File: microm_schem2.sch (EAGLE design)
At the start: 44 parts, among them IC1 DSPIC33FJ64MC804-PT, IC2 LD117AV33, IC3 7805T, IC4 RN4871-I_RM140, IC5 TB6612FNG,C,8,EL, IC6 LK112SM50TR, IC7 LK112SM33TR, Q1 16 MHz

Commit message: Update schematics and library.
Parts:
- removed C15, C16: C0805C104K4JACAUTO, SamacSys_Parts:C0805C104K4JACAUTO
- removed C21: C0805C225K4RAC3123, SamacSys_Parts:C0805C225K4RAC3123
- removed G1: AB9V, battery:AB9V
- removed IC3: 7805T, linear:7805T
- removed IC4: RN4871-I_RM140, SamacSys_Parts:RN4871-I_RM140
- removed IC6: LK112SM50TR, SamacSys_Parts:LK112SM50TR
- removed IC7: LK112SM33TR, SamacSys_Parts:LK112SM33TR
- added C1, C2: TL8W9226M010C, SamacSys_Parts:TL8W9226M010C
- added C4, C5: TAJP106K010RNJ, SamacSys_Parts:TAJP106K010RNJ
- added C6: C0805C104K4JACAUTO, SamacSys_Parts:C0805C104K4JACAUTO
- added C7: GCM21BR71A106KE22L, SamacSys_Parts:GCM21BR71A106KE22L
- added C9: 1uF, rcl:C-EUC0805
- added CON1: XT60PW-M, amass:XT60PW-M
- added IC8: LM1117DTX-5.0_NOPB, SamacSys_Parts:LM1117DTX-5.0_NOPB
- added IC9: LM1117DTX-3.3_NOPB, SamacSys_Parts:LM1117DTX-3.3_NOPB
- added LED1: APT2012MGC, SamacSys_Parts:APT2012MGC
- added LED6: APT2012VBC_D, SamacSys_Parts:APT2012VBC_D
- added R1: ERJ-PB6B2700V, rcl:R-EU_R0805
- added R2: ERJ-PB6B1001V, SamacSys_Parts:ERJ-PB6B1001V
- added R3, R4: ERJ-PB6B1002V, SamacSys_Parts:ERJ-PB6B1002V
- added S1: TS04-66-95-BK-160-SMT-TR, SamacSys_Parts:TS04-66-95-BK-160-SMT-TR
- added S2: 1101M2S3CQE2, SamacSys_Parts:1101M2S3CQE2
- C8: value 10 uF -> (none)
- IC2: value LD117AV33 -> RN4871-I_RM140; device v-reg:LD117AV33 -> SamacSys_Parts:RN4871-I_RM140
- S3, S4: value SKHMPSE010 -> TS04-66-95-BK-160-SMT-TR; device switch:SKHMPSE010 -> SamacSys_Parts:TS04-66-95-BK-160-SMT-TR
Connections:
- net AO1 renamed MA_OUT1
- net AO2 renamed MA_OUT2
- net BO1 renamed MB_OUT1
- net BO2 renamed MB_OUT2
- net BUTTON renamed BUTTON1
- net DIR_A1 renamed MA_DIR2
- net DIR_A2 renamed MA_DIR1
- net DIR_B1 renamed MB_DIR1
- net DIR_B2 renamed MB_DIR2
- net ENCA_A renamed MA_ENC_A
- net ENCA_B renamed MA_ENC_B
- net ENCB_A renamed MB_ENC_A
- net ENCB_B renamed MB_ENC_B
- net N$20 renamed SENS_DIST_3
- net N$21 renamed SENS_DIST_2
- net N$22 renamed SENS_DIST_1
- net N$5 renamed PGED1
- net N$6 renamed PGEC1
- net STDBY renamed M_STDBY
- removed net 26: IC1.AN7/RP17/CN9/RC1
- removed net 27: IC1.AN8/CVREF/RP18/PMA2/CN10/RC2
- removed net VDD3: IC5.VCC
- removed net VM: IC5.VM1
- new net BT_RESET: C9.1, IC2.RST_N, R4.1
- new net BT_STATUS: IC2.P0_2, LED6.K
- new net BUTTON2: R2.2
- new net MAB_V: C6.1, C7.1, IC5.VM1
- new net N$13: C4.+, IC8.ADJ/GND
- new net N$5: C8.1, R2.1, R3.1, S4.COM_1, S4.COM_2
- new net UART_CTS: IC2.P0_0, UART.6
- new net UART_RTS: IC2.P3_6, UART.3
- new net UART_RX: IC1.AN7/RP17/CN9/RC1, IC2.UART_RX, UART.4
- new net UART_TX: IC1.AN8/CVREF/RP18/PMA2/CN10/RC2, IC2.UART_TX, UART.5
- net +3V3: now also C2.+, IC2.VBAT, IC5.VCC, IC9.OUTPUT/VOUT, LED6.A, R3.2, R4.2, UART.1; no longer C8.1, IC2.OUT, UART.4, UART.5
- net +5V: now also C1.+, IC8.TAB_(VOUT), IC9.INPUT; no longer C15.2, C16.2, IC2.IN, IC3.VO
- net GND: now also C1.-, C17.1, C18.1, C19.1, C2.-, C20.1, C4.-, C5.-, C6.2, C7.2, C8.2, C9.2, CON1.-, IC2.GND_1, IC2.GND_2, LED1.K, S1.NO_1, S1.NO_2, S3.NO_1, S3.NO_2, S4.NO_1, S4.NO_2, UART.2; no longer S3.1.1, S3.1.2, S3.SH, S4.1.1, S4.1.2, S4.SH
- net MCLR: now also S1.COM_1, S1.COM_2; no longer S3.2.1, S3.2.2
- net N$1: now also S3.COM_1, S3.COM_2; no longer S4.2.1, S4.2.2
- net N$11: now also C5.+, IC9.ADJ/GND; no longer C15.1, C16.1, C17.1, C18.1, C19.1, C20.1, C21.1, C8.2, G1.-, IC2.ADJ, IC3.GND
- net N$2: now also CON1.+, S2.3; no longer IC1.SCL1/RP8/CN22/PMD4/RB8, UART.2
- net N$4: now also LED1.A, R1.2; no longer IC1.INT0/RP7/CN23/PMD5/RB7, UART.3
- net V+: now also IC8.INPUT, R1.1, S2.2; no longer C21.2, G1.+, IC3.VI
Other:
- note added: "Buttons"
- note added: "Distance Sensors"
- note added: "LEDs"
- note added: "Linear Voltage Regulator"
- note added: "Motor Control"
- note added: "Oscillator"
- note added: "Program Header"
- note added: "Reset Switch"
- note added: "TODO:"
- note added: "TODO: Capacitors - which ones?"
- note added: "TODO: Dummy capacitor, but need 1uF ceramic"
- note added: "TODO: Why do we need this circuit?"
- note added: "uC"
- moved on the sheet: C12, C13, C14, C17, C18, C19, C20, C22, C23, C3, C8, D2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

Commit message: Add IMU and LCD, complete wiring and clean up.
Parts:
- removed C23: C0805C200J5GACAUTO, SamacSys_Parts:C0805C200J5GACAUTO
- removed IC1: DSPIC33FJ64MC804-PT, microchip-dspic33fjxxmc:DSPIC33FJ64MC804-PT
- removed IC2: RN4871-I_RM140, SamacSys_Parts:RN4871-I_RM140
- removed IC5: TB6612FNG,C,8,EL, SamacSys_Parts:TB6612FNG,C,8,EL
- removed IC8: LM1117DTX-5.0_NOPB, SamacSys_Parts:LM1117DTX-5.0_NOPB
- removed IC9: LM1117DTX-3.3_NOPB, SamacSys_Parts:LM1117DTX-3.3_NOPB
- removed JP1, JP2, JP3: (no value), pinhead:PINHD-1X3
- removed LED1: APT2012MGC, SamacSys_Parts:APT2012MGC
- removed LED6: APT2012VBC_D, SamacSys_Parts:APT2012VBC_D
- removed R14: ERJ-PB6B1002V, SamacSys_Parts:ERJ-PB6B1002V
- removed S3, S4: TS04-66-95-BK-160-SMT-TR, SamacSys_Parts:TS04-66-95-BK-160-SMT-TR
- added 3.3V, 5V, 7.4V: green, 20mA, 2.5V, led:LEDCHIP-LED0805
- added BT_STATUS: blue, 20mA, 3.3V, led:LEDCHIP-LED0805
- added C10, C11, C15, C16, C21: 100nF, 10-20V, low-esr, rcl:C-EUC0805
- added I2C: (no value), pinhead:PINHD-1X4
- added IC3: SIP32432DR3-T1GE3, SamacSys_Parts:SIP32432DR3-T1GE3
- added IMU_1, IMU_2: (no value), pinhead:PINHD-1X6
- added LCD: (no value), pinhead:PINHD-1X11
- added LS1: CPT-9019A-SMT-TR, SamacSys_Parts:CPT-9019A-SMT-TR
- added MOTOR_CTL: TB6612FNG,C,8,EL, SamacSys_Parts:TB6612FNG,C,8,EL
- added POWER_SW: 1101M2S3CQE2, SamacSys_Parts:1101M2S3CQE2
- added R5, R6, R7: 47Ω, rcl:R-EU_R0805
- added RESET: TS04-66-95-BK-160-SMT-TR, SamacSys_Parts:TS04-66-95-BK-160-SMT-TR
- added SENS_DIST_1, SENS_DIST_2, SENS_DIST_3: (no value), pinhead:PINHD-1X3
- added SPI: (no value), pinhead:PINHD-2X4
- added TP_3.3V, TP_5V, TP_7.4V, TP_GND, TP_OSC: (no value), pinhead:PINHD-1X1
- added UART_BT: RN4871-I_RM140, SamacSys_Parts:RN4871-I_RM140
- added UC: DSPIC33FJ64MC804-PT, microchip-dspic33fjxxmc:DSPIC33FJ64MC804-PT
- added VR_3.3V: LM1117DTX-3.3_NOPB, SamacSys_Parts:LM1117DTX-3.3_NOPB
- added VR_5V: LM1117DTX-5.0_NOPB, SamacSys_Parts:LM1117DTX-5.0_NOPB
- C1: value TL8W9226M010C -> 10uF, tantalum; device SamacSys_Parts:TL8W9226M010C -> rcl:C-EUC0805
- C12, C13, C14: value (none) -> 10 uF
- C17, C18: value C0805C104K4JACAUTO -> 20pF, low-esr, ceramic; device SamacSys_Parts:C0805C104K4JACAUTO -> rcl:C-EUC0805
- C19, C6: value C0805C104K4JACAUTO -> 100nF; device SamacSys_Parts:C0805C104K4JACAUTO -> rcl:C-EUC0805
- C2: value TL8W9226M010C -> 22uF, tantalum, esr 0.3-22Ω; device SamacSys_Parts:TL8W9226M010C -> rcl:C-EUC0805
- C20: value C0805C104K4JACAUTO -> 10uF; device SamacSys_Parts:C0805C104K4JACAUTO -> rcl:C-EUC0805
- C22: value C0805C200J5GACAUTO -> 100nF, 10-20V, low-esr; device SamacSys_Parts:C0805C200J5GACAUTO -> rcl:C-EUC0805
- C3, C8: value (none) -> 100nF
- C4: value TAJP106K010RNJ -> 10uF, tantalum; device SamacSys_Parts:TAJP106K010RNJ -> rcl:C-EUC0805
- C5: value TAJP106K010RNJ -> 22uF, tantalum, esr 0.3-22Ω; device SamacSys_Parts:TAJP106K010RNJ -> rcl:C-EUC0805
- C7: value GCM21BR71A106KE22L -> 10uF; device SamacSys_Parts:GCM21BR71A106KE22L -> rcl:C-EUC0805
- LED2, LED3, LED4, LED5: value (none) -> red, 20mA, 2.5V
- R1: value ERJ-PB6B2700V -> 270Ω
- R10, R3, R4, R9: value ERJ-PB6B1002V -> 10kΩ; device SamacSys_Parts:ERJ-PB6B1002V -> rcl:R-EU_R0805
- R11: value ERJ-PB6B1002V -> 47Ω; device SamacSys_Parts:ERJ-PB6B1002V -> rcl:R-EU_R0805
- R12, R13: value ERJ-PB6B1002V -> 270Ω; device SamacSys_Parts:ERJ-PB6B1002V -> rcl:R-EU_R0805
- R2, R8: value ERJ-PB6B1001V -> 1kΩ; device SamacSys_Parts:ERJ-PB6B1001V -> rcl:R-EU_R0805
- S2: value 1101M2S3CQE2 -> TS04-66-95-BK-160-SMT-TR; device SamacSys_Parts:1101M2S3CQE2 -> SamacSys_Parts:TS04-66-95-BK-160-SMT-TR
- UART: value MICS-SMD06 -> (none); device con-lumberg:MICS-SMD06 -> pinhead:PINHD-1X4
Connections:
- removed net 1: IC1.SDA1/RP9/CN21/PMD3/RB9
- removed net 11: IC1.PWM1L2/DAC1RN/RP13/CN13/PMRD/RB13
- removed net 12: IC1.TMS/PMA10/RA10
- removed net 15: IC1.PWM1L1/RP15/CN11/PMCS1/RB15
- removed net 2: IC1.PWM2H1/RP22/CN18/PMA1/RC6
- removed net 23: IC1.AN4/C1IN-/RP2/CN6/RB2
- removed net 24: IC1.AN5/C1IN+/RP3/CN7/RB3
- removed net 25: IC1.AN6/RP16/CN8/RC0
- removed net 3: IC1.PWM2L1/RP23/CN17/PMA0/RC7
- removed net 34: IC1.SOSCO/T1CK/CN0/RA4
- removed net 35: IC1.TDI/PMA9/RA9
- removed net MAB_V: C6.1, C7.1, IC5.VM1
- removed net N$12: IC1.AN0/VREF+/CN2/RA0
- removed net N$14: IC5.VM2
- removed net N$15: IC5.VM3
- removed net N$29: MOTOR_B.4
- removed net N$5: C8.1, R2.1, R3.1, S4.COM_1, S4.COM_2
- removed net PGEC1: IC1.PGEC1/AN3/C2IN+/RP1/CN5/RB1, PROGRAM.5
- removed net PGED1: IC1.PGED1/AN2/C2IN-/RP0/CN4/RB0, PROGRAM.4
- removed net UART_CTS: IC2.P0_0, UART.6
- removed net UART_RTS: IC2.P3_6, UART.3
- removed net V+: IC8.INPUT, R1.1, S2.2
- removed net VDD33: MOTOR_A.4
- new net +7V4: POWER_SW.2, R1.1, TP_7.4V.1, VR_5V.INPUT
- new net AGND: UC.AVSS
- new net BUZZ_PWM: LS1.+, UC.PWM2H1/RP22/CN18/PMA1/RC6
- new net GND1: 5V.C
- new net GND2: 3.3V.C
- new net I2C_SCL: I2C.1, IMU_2.4, UC.SCL1/RP8/CN22/PMD4/RB8
- new net I2C_SDA: I2C.2, IMU_2.5, UC.SDA1/RP9/CN21/PMD3/RB9
- new net IMU_INT: IMU_2.6, UC.INT0/RP7/CN23/PMD5/RB7
- new net LCD_BL_PWM: LCD.11, UC.PGED2/PWM1H3/RP10/CN16/PMD2/RB10
- new net LCD_RESET: LCD.8, UC.SOSCI/RP4/CN1/RB4
- new net M_3V3: MOTOR_CTL.VCC
- new net M_7V4: C6.1, C7.1, MOTOR_CTL.VM1, MOTOR_CTL.VM2, MOTOR_CTL.VM3
- new net N$16: 5V.A, R12.2
- new net N$17: 3.3V.A, R13.2
- new net N$6: C3.1, R8.1, R9.1, S1.COM_1, S1.COM_2
- new net PG_EC1: PROGRAM.5, UC.PGEC1/AN3/C2IN+/RP1/CN5/RB1
- new net PG_ED1: PROGRAM.4, UC.PGED1/AN2/C2IN-/RP0/CN4/RB0
- new net SENS_DIST_ON: IC3.ON/OFF, UC.TDO/PMA8/RA8
- new net SENS_DIST_V: C12.1, C13.1, C14.1, IC3.OUT, SENS_DIST_1.1, SENS_DIST_2.1, SENS_DIST_3.1
- new net SPI_DBG_CS: SPI.6
- new net SPI_LCD_CS: LCD.7, SPI.2, UC.AN6/RP16/CN8/RC0
- new net SPI_LCD_DC: LCD.9, UC.AN8/CVREF/RP18/PMA2/CN10/RC2
- new net SPI_SCK: LCD.4, SPI.1, UC.PGEC2/PWM1L3/RP11/CN15/PMD1/RB11
- new net SPI_SDI: LCD.6, SPI.5, UC.PWM1L2/DAC1RN/RP13/CN13/PMRD/RB13
- new net SPI_SDO: LCD.5, SPI.3, UC.PWM1L1/RP15/CN11/PMCS1/RB15
- new net SPI_SD_CS: LCD.10, SPI.4
- net +3V3: now also BT_STATUS.C, C10.1, C11.1, C15.1, C16.1, C19.1, C20.1, C21.1, C22.1, C5.1, I2C.4, IMU_2.1, LCD.1, MOTOR_A.4, MOTOR_B.4, R11.1, R13.1, R5.1, R6.1, R7.1, SPI.7, TP_3.3V.1, UART.4, UART_BT.VBAT, UC.AVDD, UC.VCAP/VDDCORE, UC.VDD, UC.VDD1, VR_3.3V.OUTPUT/VOUT; no longer C17.2, C18.2, C19.2, C2.+, C20.2, IC1.AVDD, IC1.VCAP/VDDCORE, IC1.VDD, IC1.VDD1, IC2.VBAT, IC5.VCC, IC9.OUTPUT/VOUT, LED6.A, R11.2, R12.2, R13.2, R14.2, UART.1
- net +5V: now also C2.1, IC3.IN, R12.1, TP_5V.1, VR_3.3V.INPUT, VR_5V.TAB_(VOUT); no longer C1.+, C12.1, C13.1, C14.1, IC8.TAB_(VOUT), IC9.INPUT, JP1.1, JP2.1, JP3.1
- net 0SC2: now also C18.1, TP_OSC.1; no longer C22.2
- net BT_RESET: now also UART_BT.RST_N; no longer IC2.RST_N
- net BT_STATUS: now also BT_STATUS.A, UART_BT.P0_2; no longer IC2.P0_2, LED6.K
- net BUTTON1: now also UC.PWM2L1/RP23/CN17/PMA0/RC7
- net GND: now also 7.4V.C, C1.2, C10.2, C11.2, C15.2, C16.2, C17.2, C18.2, C19.2, C2.2, C20.2, C21.2, C22.2, C4.2, C5.2, I2C.3, IC3.GND_1, IC3.GND_2, IMU_1.4, IMU_2.3, LCD.3, LS1.-, MOTOR_CTL.GND, MOTOR_CTL.PGND1_1, MOTOR_CTL.PGND1_2, MOTOR_CTL.PGND2_1, MOTOR_CTL.PGND2_2, RESET.NO_1, RESET.NO_2, S2.NO_1, S2.NO_2, SENS_DIST_1.2, SENS_DIST_2.2, SENS_DIST_3.2, SPI.8, TP_GND.1, UART.3, UART_BT.GND_1, UART_BT.GND_2, UC.VSS, UC.VSS1, UC.VSS2; no longer C1.-, C17.1, C18.1, C19.1, C2.-, C20.1, C22.1, C23.1, C4.-, C5.-, IC1.AVSS, IC1.VSS, IC1.VSS1, IC1.VSS2, IC2.GND_1, IC2.GND_2, IC5.GND, IC5.PGND1_1, IC5.PGND1_2, IC5.PGND2_1, IC5.PGND2_2, JP1.2, JP2.2, JP3.2, LED1.K, S3.NO_1, S3.NO_2, S4.NO_1, S4.NO_2, UART.2
- net LED1: now also UC.AN0/VREF+/CN2/RA0
- net LED2: now also UC.AN1/VREF-/CN3/RA1
- net MA_DIR1: now also MOTOR_CTL.AIN1, UC.TMS/PMA10/RA10; no longer IC5.AIN1
- net MA_DIR2: now also MOTOR_CTL.AIN2, UC.TCK/PMA7/RA7; no longer IC5.AIN2
- net MA_ENC_A: now also UC.RP19/CN28/PMBE/RC3; no longer IC1.RP19/CN28/PMBE/RC3
- net MA_ENC_B: now also UC.RP20/CN25/PMA4/RC4; no longer IC1.RP20/CN25/PMA4/RC4
- net MA_OUT1: now also MOTOR_CTL.AO1_1, MOTOR_CTL.AO1_2; no longer IC5.AO1_1, IC5.AO1_2
- net MA_OUT2: now also MOTOR_CTL.AO2_1, MOTOR_CTL.AO2_2; no longer IC5.AO2_1, IC5.AO2_2
- net MA_PWM: now also MOTOR_CTL.PWMA, UC.PWM1H1/RTCC/RP14/CN12/PMWR/RB14; no longer IC1.PWM1H1/RTCC/RP14/CN12/PMWR/RB14, IC5.PWMA
- net MB_DIR1: now also MOTOR_CTL.BIN1, UC.SOSCO/T1CK/CN0/RA4; no longer IC5.BIN1
- net MB_DIR2: now also MOTOR_CTL.BIN2, UC.TDI/PMA9/RA9; no longer IC5.BIN2
- net MB_ENC_A: now also UC.RP24/CN20/PMA5/RC8; no longer IC1.RP24/CN20/PMA5/RC8
- net MB_ENC_B: now also UC.RP25/CN19/PMA6/RC9; no longer IC1.RP25/CN19/PMA6/RC9
- net MB_OUT1: now also MOTOR_CTL.BO1_1, MOTOR_CTL.BO1_2; no longer IC5.BO1_1, IC5.BO1_2
- net MB_OUT2: now also MOTOR_CTL.BO2_1, MOTOR_CTL.BO2_2; no longer IC5.BO2_1, IC5.BO2_2
- net MB_PWM: now also MOTOR_CTL.PWMB, UC.PWM1H2/DAC1RP/RP12/CN14/PMD0/RB12; no longer IC1.PWM1H2/DAC1RP/RP12/CN14/PMD0/RB12, IC5.PWMB
- net MCLR: now also RESET.COM_1, RESET.COM_2, UC.MCLR; no longer IC1.MCLR, S1.COM_1, S1.COM_2
- net M_STDBY: now also MOTOR_CTL.STBY, UC.RP21/CN26/PMA3/RC5; no longer IC1.RP21/CN26/PMA3/RC5, IC5.STBY
- net N$1: now also C8.1, R2.1, R3.1, S2.COM_1, S2.COM_2; no longer C3.1, R8.1, R9.1, S3.COM_1, S3.COM_2
- net N$10: now also R11.2; no longer R14.1
- net N$11: now also C4.1, VR_3.3V.ADJ/GND; no longer C5.+, IC9.ADJ/GND
- net N$13: now also C1.1, VR_5V.ADJ/GND; no longer C4.+, IC8.ADJ/GND
- net N$2: now also POWER_SW.3; no longer S2.3
- net N$3: now also R5.2; no longer R11.1
- net N$4: now also 7.4V.A; no longer LED1.A
- net N$8: now also R6.2; no longer R12.1
- net N$9: now also R7.2; no longer R13.1
- net OSC1: now also C17.1, UC.OSC1/CLKI/CN30/RA2; no longer C23.2, IC1.OSC1/CLKI/CN30/RA2
- net OSC2: now also UC.OSC2/CLKO/CN29/RA3; no longer IC1.OSC2/CLKO/CN29/RA3
- net SENS_DIST_1: now also SENS_DIST_1.3, UC.AN4/C1IN-/RP2/CN6/RB2; no longer JP1.3
- net SENS_DIST_2: now also SENS_DIST_2.3, UC.AN5/C1IN+/RP3/CN7/RB3; no longer JP2.3
- net SENS_DIST_3: now also SENS_DIST_3.3, UC.AN7/RP17/CN9/RC1; no longer JP3.3
- net UART_RX: now also UART.1, UART_BT.UART_RX, UC.PGED3/ASDA1/RP5/CN27/PMD7/RB5; no longer IC1.AN7/RP17/CN9/RC1, IC2.UART_RX, UART.4
- net UART_TX: now also UART.2, UART_BT.UART_TX, UC.PGEC3/ASCL1/RP6/CN24/PMD6/RB6; no longer IC1.AN8/CVREF/RP18/PMA2/CN10/RC2, IC2.UART_TX, UART.5
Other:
- note added: "4x uC, 2x QEA"
- note added: "Debug Interfaces"
- note added: "IMU Header"
- note added: "LCD Header"
- note added: "Piezo Buzzer"
- note added: "TODO: Transistor/Load Switch correct?"
- note added: "UART"
- note removed: "TODO: Dummy capacitor, but need 1uF ceramic"
- moved on the sheet: C12, C13, C14, C3, C8, C9, CON1, D2, LED2, LED3, LED4, LED5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

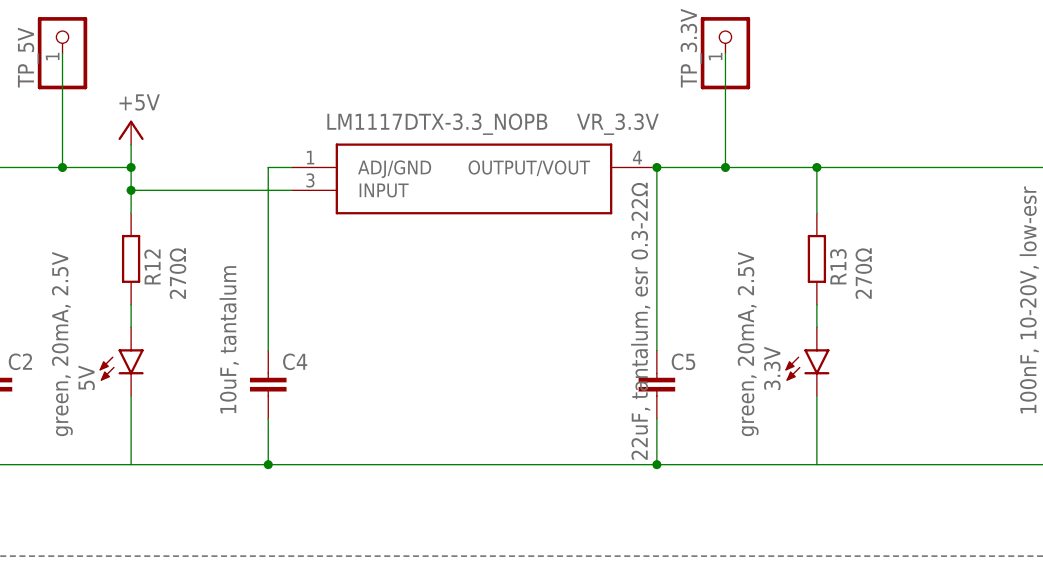
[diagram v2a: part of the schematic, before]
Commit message: Fix led resitors.
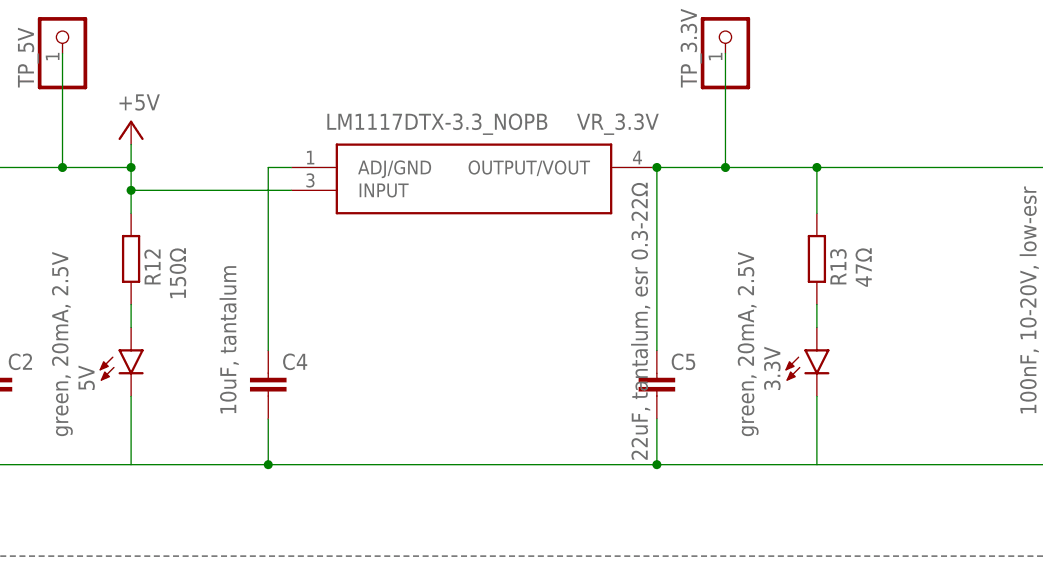
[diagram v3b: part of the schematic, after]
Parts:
- R12: value 270Ω -> 150Ω
- R13: value 270Ω -> 47Ω
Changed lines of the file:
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@@
 <part name="GND32" library="supply1" library_urn="urn:adsk.eagle:library:371" deviceset="GND" device=""/>
 <part name="UART" library="pinhead" library_urn="urn:adsk.eagle:library:325" deviceset="PINHD-1X4" device="" package3d_urn="urn:adsk.eagle:package:22407/2"/>
-<part name="R12" library="rcl" library_urn="urn:adsk.eagle:library:334" deviceset="R-EU_" device="R0805" package3d_urn="urn:adsk.eagle:package:23553/2" value="270Ω"/>
+<part name="R12" library="rcl" library_urn="urn:adsk.eagle:library:334" deviceset="R-EU_" device="R0805" package3d_urn="urn:adsk.eagle:package:23553/2" value="150Ω"/>
 <part name="5V" library="led" library_urn="urn:adsk.eagle:library:259" deviceset="LED" device="CHIP-LED0805" package3d_urn="urn:adsk.eagle:package:15818/2" value="green, 20mA, 2.5V"/>
-<part name="R13" library="rcl" library_urn="urn:adsk.eagle:library:334" deviceset="R-EU_" device="R0805" package3d_urn="urn:adsk.eagle:package:23553/2" value="270Ω"/>
+<part name="R13" library="rcl" library_urn="urn:adsk.eagle:library:334" deviceset="R-EU_" device="R0805" package3d_urn="urn:adsk.eagle:package:23553/2" value="47Ω"/>
 <part name="3.3V" library="led" library_urn="urn:adsk.eagle:library:259" deviceset="LED" device="CHIP-LED0805" package3d_urn="urn:adsk.eagle:package:15818/2" value="green, 20mA, 2.5V"/>
 <part name="BT_STATUS" library="led" library_urn="urn:adsk.eagle:library:259" deviceset="LED" device="CHIP-LED0805" package3d_urn="urn:adsk.eagle:package:15818/2" value="blue, 20mA, 3.3V"/>

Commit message: Fix ERC issues and add mounting pads.
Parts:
- added H1, H2, H3, H4, H5, H6, H7, H8: 2.8, holes:MOUNT-PAD-SQUARE2.8
- added R14: 0Ω, rcl:R-EU_R0805
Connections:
- removed net 0SC2: C18.1, Q1.2, TP_OSC.1
- removed net GND1: 5V.C
- removed net GND2: 3.3V.C
- removed net M_3V3: MOTOR_CTL.VCC
- removed net M_7V4: C6.1, C7.1, MOTOR_CTL.VM1, MOTOR_CTL.VM2, MOTOR_CTL.VM3
- removed net SPI_DBG_CS: SPI.6
- net +3V3: now also MOTOR_CTL.VCC
- net +7V4: now also C6.1, C7.1, MOTOR_CTL.VM1, MOTOR_CTL.VM2, MOTOR_CTL.VM3
- net AGND: now also R14.2
- net GND: now also 3.3V.C, 5V.C, H1.MOUNT, H2.MOUNT, H3.MOUNT, H4.MOUNT, H5.MOUNT, H6.MOUNT, H7.MOUNT, H8.MOUNT, R14.1
- net MA_ENC_A: now also MOTOR_A.6; no longer MOTOR_A.5
- net MA_ENC_B: now also MOTOR_A.5; no longer MOTOR_A.6
- net MA_OUT1: now also MOTOR_A.2; no longer MOTOR_A.1
- net MA_OUT2: now also MOTOR_A.1; no longer MOTOR_A.2
- net OSC2: now also C18.1, Q1.2, TP_OSC.1
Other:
- note added: "Hack: Fix ERC"
- note added: "Note: Reversed Voltage and QEI PINs as wheel is mounted in reverse position."
- moved on the sheet: IMU_1, IMU_2

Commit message: Add first version of the PCB.
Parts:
- removed H3, H4, H5, H6, H7, H8: 2.8, holes:MOUNT-PAD-SQUARE2.8
- removed LED5: red, 20mA, 2.5V, led:LEDCHIPLED_0805
- added LED1: red, 20mA, 2.5V, led:LEDCHIPLED_0805
- H1, H2: value 2.8 -> MOUNT-PAD-ROUND2.8; device holes:MOUNT-PAD-SQUARE2.8 -> holes:MOUNT-PAD-ROUND2.8
- PROGRAM: value MICS-SMD06 -> (none); device con-lumberg:MICS-SMD06 -> pinhead:PINHD-1X6/90
- renumbered CON1 to BAT, IC3 to T1, TP_3.3V to TP3V3, TP_5V to TP5V, TP_7.4V to TP7V4, TP_GND to TPGND
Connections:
- net GND: no longer H3.MOUNT, H4.MOUNT, H5.MOUNT, H6.MOUNT, H7.MOUNT, H8.MOUNT
- net LED1: now also LED1.C; no longer LED2.C
- net LED2: now also LED2.C; no longer LED5.C
- net N$3: now also LED1.A; no longer LED2.A
- net N$8: now also LED2.A; no longer LED5.A
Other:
- moved on the sheet: LED2

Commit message: Add changes from meeting today.
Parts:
- removed C8: 100nF, rcl:C-EUC0805
- removed LED3, LED4: red, 20mA, 2.5V, led:LEDCHIPLED_0805
- removed R11, R7: 47Ω, rcl:R-EU_R0805
- removed R2: 1kΩ, rcl:R-EU_R0805
- removed R3: 10kΩ, rcl:R-EU_R0805
- removed S2: TS04-66-95-BK-160-SMT-TR, SamacSys_Parts:TS04-66-95-BK-160-SMT-TR
- removed T1: SIP32432DR3-T1GE3, SamacSys_Parts:SIP32432DR3-T1GE3
- added BT_RST: (no value), pinhead:PINHD-1X2
- added RX_SEL: (no value), pinhead:PINHD-1X3
- renumbered RESET to µC_RST
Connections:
- removed net BUTTON2: R2.2
- removed net LED3: LED3.C
- removed net LED4: LED4.C
- removed net N$1: C8.1, R2.1, R3.1, S2.COM_1, S2.COM_2
- removed net N$10: LED4.A, R11.2
- removed net N$9: LED3.A, R7.2
- removed net SENS_DIST_ON: T1.ON/OFF, UC.TDO/PMA8/RA8
- removed net SENS_DIST_V: C12.1, C13.1, C14.1, SENS_DIST_1.1, SENS_DIST_2.1, SENS_DIST_3.1, T1.OUT
- new net UART_BT_RX: RX_SEL.1, UART_BT.UART_RX
- new net UART_DBG_RX: RX_SEL.3, UART.1
- net +3V3: no longer R11.1, R3.2, R7.1
- net +5V: now also C12.1, C13.1, C14.1, SENS_DIST_1.1, SENS_DIST_2.1, SENS_DIST_3.1; no longer T1.IN
- net BT_RESET: now also BT_RST.1
- net GND: now also BT_RST.2; no longer C8.2, S2.NO_1, S2.NO_2, T1.GND_1, T1.GND_2
- net UART_RX: now also RX_SEL.2; no longer UART.1, UART_BT.UART_RX
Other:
- note removed: "TODO: Capacitors - which ones?"
- note removed: "TODO: Transistor/Load Switch correct?"
- note removed: "TODO: Why do we need this circuit?"
- moved on the sheet: C12, C13, C14, C3, C9, R4, R8, R9, S1, SENS_DIST_1, SENS_DIST_2, SENS_DIST_3

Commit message: Update schematic.
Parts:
- removed BT_STATUS: blue, 20mA, 3.3V, led:LEDCHIP-LED0805
- removed R14: 0Ω, rcl:R-EU_R0805
- removed TP_OSC: (no value), pinhead:PINHD-1X1
- added BT_CON: blue, 2mA, 3V, led:LEDCHIP-LED0805
- added BT_PROG: (no value), pinhead:PINHD-1X2
- added C8: 10uF, rcl:C-EUC0805
- added H3, H4, H5, H6, H7, H8: MOUNT-PAD-ROUND2.8, holes:MOUNT-PAD-ROUND2.8
- added L1: 47uH, rcl:L-EUL1812
- added R11: 1kΩ, rcl:R-EU_R0805
- added R2: 1.2kΩ, rcl:R-EU_R0805
- added R3: 180Ω, rcl:R-EU_R0805
- added R7: 2.2kΩ, rcl:R-EU_R0805
- 3.3V, 5V, 7.4V: value green, 20mA, 2.5V -> green, 2mA, 3V
- C12, C13, C14: value 10 uF -> 100nF, 10-20V, low-esr
- C15, C16: value 100nF, 10-20V, low-esr -> 20pF, low-esr, ceramic
- C17, C18: value 20pF, low-esr, ceramic -> 10 uF
- C19: value 100nF -> 10 uF
- C20: value 10uF -> 1uF
- C21: value 100nF, 10-20V, low-esr -> 1uF
- C22: value 100nF, 10-20V, low-esr -> 100nF
- C3: value 100nF -> 10uF, tantalum
- C4: value 10uF, tantalum -> 22uF, tantalum, esr 0.3-22Ω
- C5: value 22uF, tantalum, esr 0.3-22Ω -> 100nF
- C6: value 100nF -> 10uF
- C7: value 10uF -> 100nF
- C9: value 1uF -> 100nF, 10-20V, low-esr
- LED1, LED2: value red, 20mA, 2.5V -> red, 2mA, 2.1V
- R1: value 270Ω -> 2.7kΩ
- R12: value 150Ω -> 10kΩ
- R13: value 47Ω -> 10kΩ
- R4: value 10kΩ -> 680Ω
- R5: value 47Ω -> 680Ω
- R6: value 47Ω -> 180Ω
- R8: value 1kΩ -> 2.2kΩ
- renumbered PROGRAM to UC_PROG, TP3V3 to T3.3V, TP5V to T5V, TP7V4 to T7.4V, TPGND to TGND
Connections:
- removed net AGND: R14.2, UC.AVSS
- removed net N$11: C4.1, VR_3.3V.ADJ/GND
- removed net N$13: C1.1, VR_5V.ADJ/GND
- new net BT_PROG: BT_PROG.1, C21.1, R12.1, UART_BT.P2_0
- new net N$1: BT_CON.A, R6.2
- new net N$5: C14.2, L1.1, UC.AVDD
- new net UART_BT_RX_IND: UART_BT.P1_6
- net +3V3: now also BT_CON.C, C12.1, C13.1, C4.1, C7.1, C8.1, C9.1, L1.2, R10.2, R12.2, R13.2, R3.1, R4.1, R7.1, R8.1; no longer BT_STATUS.C, C15.1, C16.1, C19.1, C20.1, C21.1, C22.1, C5.1, R13.1, R4.2, R6.1, R9.2, UC.AVDD
- net +5V: now also C17.1, C18.1, C19.1, C3.1, R2.1; no longer C12.1, C13.1, C14.1, R12.1
- net +7V4: now also C1.1, C5.1; no longer C7.1
- net BT_RESET: now also C20.1, R13.1; no longer C9.1, R4.1
- net BT_STATUS: now also R6.1; no longer BT_STATUS.A
- net BUTTON1: now also R11.2; no longer R8.2
- net GND: now also BT_PROG.2, C14.1, C8.2, H3.MOUNT, H4.MOUNT, H5.MOUNT, H6.MOUNT, H7.MOUNT, H8.MOUNT, UC.AVSS, VR_3.3V.ADJ/GND, VR_5V.ADJ/GND; no longer C14.2, R14.1
- net I2C_SCL: now also R7.2
- net I2C_SDA: now also R8.2
- net MCLR: now also R9.1; no longer R10.1
- net N$16: now also R2.2; no longer R12.2
- net N$17: now also R3.2; no longer R13.2
- net N$3: now also R4.2; no longer R5.2
- net N$6: now also C22.1, R10.1, R11.1; no longer C3.1, R8.1, R9.1
- net N$7: now also R9.2; no longer R10.2
- net N$8: now also R5.2; no longer R6.2
- net OSC1: now also C15.1; no longer C17.1
- net OSC2: now also C16.1; no longer C18.1, TP_OSC.1
- net UART_BT_RX: now also UART_BT.UART_TX; no longer UART_BT.UART_RX
- net UART_TX: now also UART_BT.UART_RX; no longer UART_BT.UART_TX
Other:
- note added: "3x uC (AVdd is separate), 2x QEA"
- note added: "I2C Pull-Up Resistors Only in case lower resistance is needed"
- note added: "Mounting Holes (Sensors / Motors)"
- note removed: "4x uC, 2x QEA"
- note removed: "Hack: Fix ERC"
- moved on the sheet: BT_RST, C1, C10, C11, C12, C13, C14, C15, C16, C17, C18, C19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
